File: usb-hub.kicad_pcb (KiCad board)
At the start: 4 copper layers, 23.4 x 28.4 mm, 64 parts, among them J1 USB_C_Receptacle_16pin, J2 USB_C_Receptacle_16pin, J3 USB_C_Receptacle_16pin, J4 Conn_01x01_Female, J5 Conn_01x01_Female, J6 Conn_01x01_Female, J7 Conn_01x01_Female, Q1 PMOS, -3.6A, 0.02R, Q2 Q_NMOS_GSD 1Amp, SW1 SW_Push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

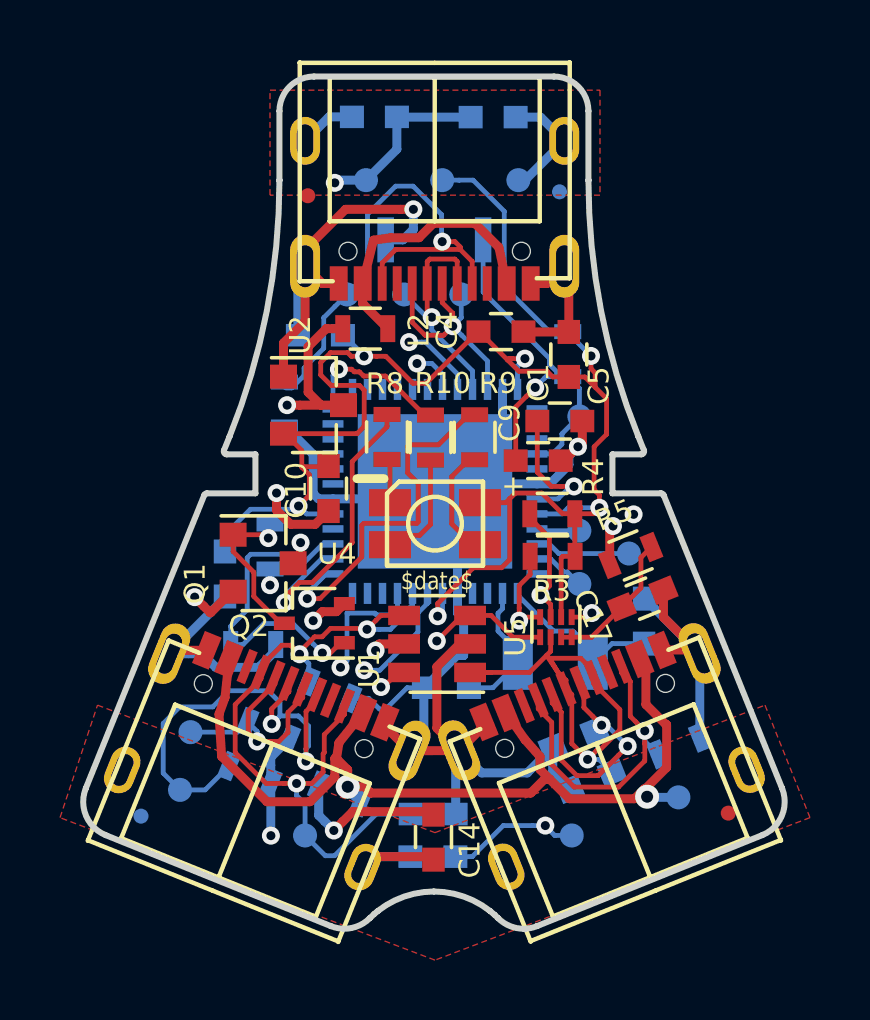
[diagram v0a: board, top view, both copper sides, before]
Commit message: improve clarity of polarity of u5
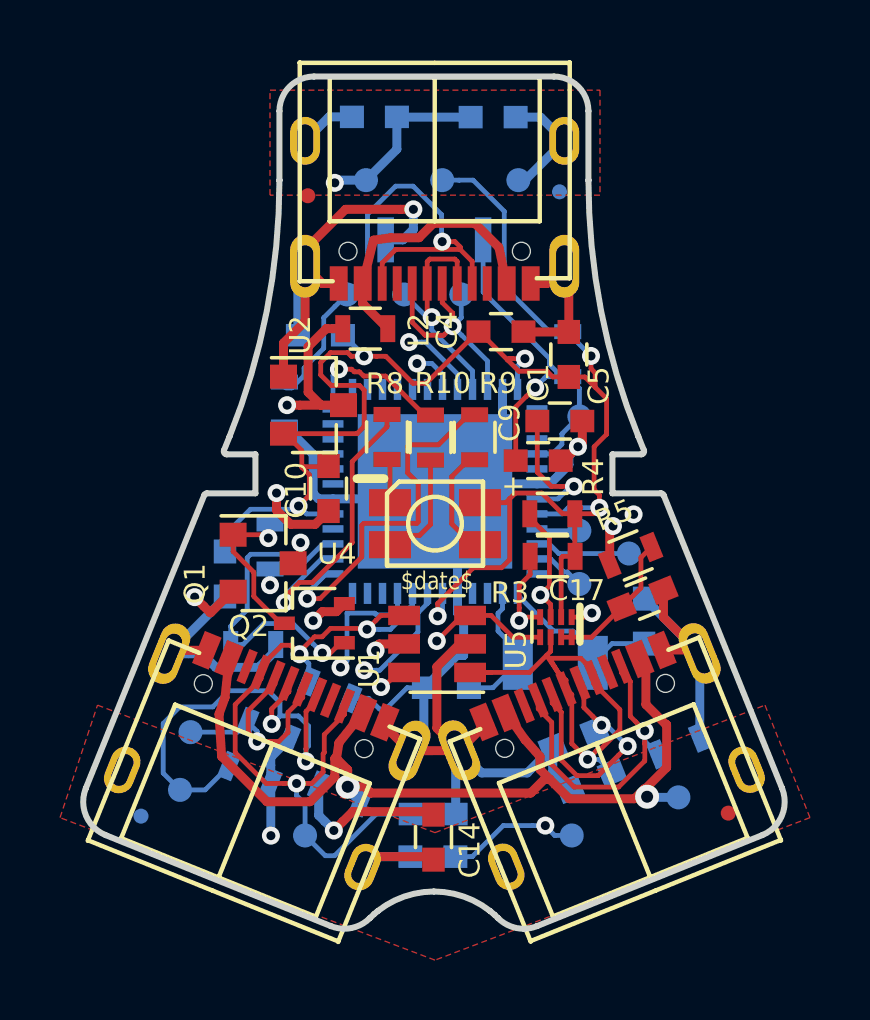
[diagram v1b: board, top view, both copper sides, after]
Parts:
- U5: footprint Housings_SON:X2SON-8_1.4x1mm_Pitch0.35mm -> X2SON-8_1.4x1mm_Pitch0.35mm
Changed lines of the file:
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@@
     (add_net /side-power)
+  )
+  (module X2SON-8_1.4x1mm_Pitch0.35mm (layer F.Cu)
+    (at 146.03 110.15 270)
+    (descr "X2SON-8 1.4x1mm Pitch0.35mm http://www.ti.com/lit/ds/symlink/pca9306.pdf")
+    (tags "X2SON-8 1.4x1mm Pitch0.35mm")
+    (attr smd)
+    (fp_text reference U5 (at 0.75 1.33 90) (layer F.SilkS)
+      (effects (font (size 0.7 0.7) (thickness 0.1)))
+    )
+    (fp_text value pca9306 (at 0 2 270) (layer F.Fab)
+      (effects (font (size 1 1) (thickness 0.15)))
+    )
+    (fp_text user %R (at 0 0) (layer F.Fab)
+      (effects (font (size 0.3 0.3) (thickness 0.05)))
+    )
+    (fp_line (start -0.85 -0.95) (end 0.85 -0.95) (layer F.CrtYd) (width 0.05))
+    (fp_line (start -0.85 0.95) (end -0.85 -0.95) (layer F.CrtYd) (width 0.05))
+    (fp_line (start 0.85 0.95) (end -0.85 0.95) (layer F.CrtYd) (width 0.05))
+    (fp_line (start 0.85 -0.95) (end 0.85 0.95) (layer F.CrtYd) (width 0.05))
+    (fp_line (start 0.5 0.8) (end -0.5 0.8) (layer F.SilkS) (width 0.12))
+    (fp_line (start 0.5 -0.8) (end -0.7 -0.8) (layer F.SilkS) (width 0.25))
+    (fp_line (start 0 -0.7) (end -0.5 -0.2) (layer F.Fab) (width 0.1))
+    (fp_line (start 0 -0.7) (end 0.5 -0.7) (layer F.Fab) (width 0.1))
+    (fp_line (start -0.5 0.7) (end -0.5 -0.2) (layer F.Fab) (width 0.1))
+    (fp_line (start 0.5 0.7) (end -0.5 0.7) (layer F.Fab) (width 0.1))
+    (fp_line (start 0.5 -0.7) (end 0.5 0.7) (layer F.Fab) (width 0.1))
+    (pad 1 smd rect (at -0.335 -0.525 180) (size 0.2 0.53) (layers F.Cu F.Paste F.Mask)
+      (net 1 Earth))
+    (pad 2 smd rect (at -0.335 -0.175 180) (size 0.2 0.53) (layers F.Cu F.Paste F.Mask)
+      (net 3 +3V3))
+    (pad 3 smd rect (at -0.335 0.175 180) (size 0.2 0.53) (layers F.Cu F.Paste F.Mask)
+      (net 58 /scl33))
+    (pad 4 smd rect (at -0.335 0.525 180) (size 0.2 0.53) (layers F.Cu F.Paste F.Mask)
+      (net 57 /sda33))
+    (pad 5 smd rect (at 0.335 0.525 180) (size 0.2 0.53) (layers F.Cu F.Paste F.Mask)
+      (net 22 /sda))
+    (pad 6 smd rect (at 0.335 0.175 180) (size 0.2 0.53) (layers F.Cu F.Paste F.Mask)
+      (net 23 /scl))
+    (pad 7 smd rect (at 0.335 -0.175 180) (size 0.2 0.53) (layers F.Cu F.Paste F.Mask)
+      (net 56 "Net-(C17-Pad2)"))
+    (pad 8 smd rect (at 0.335 -0.525 180) (size 0.2 0.53) (layers F.Cu F.Paste F.Mask)
+      (net 56 "Net-(C17-Pad2)"))
+    (model ${KISYS3DMOD}/Housings_SON.3dshapes/X2SON-8_1.4x1mm_Pitch0.35mm.wrl
+      (at (xyz 0 0 0))
+      (scale (xyz 1 1 1))
+      (rotate (xyz 0 0 0))
+    )
   )
   (module raise_fp:usb-c-16smt (layer F.Cu)
@@
     (tags "resistor 0603")
     (attr smd)
-    (fp_text reference R3 (at -0.03 1.15) (layer F.SilkS)
+    (fp_text reference R3 (at -1.42 1.21) (layer F.SilkS)
       (effects (font (size 0.7 0.7) (thickness 0.1)))
     )
@@
     (tags "capacitor 0603")
     (attr smd)
-    (fp_text reference C17 (at 1.776907 0.060011 292) (layer F.SilkS)
+    (fp_text reference C17 (at 1.932152 1.077237 180) (layer F.SilkS)
       (effects (font (size 0.7 0.7) (thickness 0.1)))
     )
@@
       (net 23 /scl))
     (model ${KIPRJMOD}/raise_fp.pretty/models/R_0603_1608Metric.wrl
-      (at (xyz 0 0 0))
-      (scale (xyz 1 1 1))
-      (rotate (xyz 0 0 0))
-    )
-  )
-  (module Housings_SON:X2SON-8_1.4x1mm_Pitch0.35mm (layer F.Cu)
-    (at 146.03 110.15 270)
-    (descr "X2SON-8 1.4x1mm Pitch0.35mm http://www.ti.com/lit/ds/symlink/pca9306.pdf")
-    (tags "X2SON-8 1.4x1mm Pitch0.35mm")
-    (attr smd)
-    (fp_text reference U5 (at 0.33 1.35 90) (layer F.SilkS)
-      (effects (font (size 0.7 0.7) (thickness 0.1)))
-    )
-    (fp_text value pca9306 (at 0 2 270) (layer F.Fab)
-      (effects (font (size 1 1) (thickness 0.15)))
-    )
-    (fp_text user %R (at 0 0) (layer F.Fab)
-      (effects (font (size 0.3 0.3) (thickness 0.05)))
-    )
-    (fp_line (start -0.85 -0.95) (end 0.85 -0.95) (layer F.CrtYd) (width 0.05))
-    (fp_line (start -0.85 0.95) (end -0.85 -0.95) (layer F.CrtYd) (width 0.05))
-    (fp_line (start 0.85 0.95) (end -0.85 0.95) (layer F.CrtYd) (width 0.05))
-    (fp_line (start 0.85 -0.95) (end 0.85 0.95) (layer F.CrtYd) (width 0.05))
-    (fp_line (start 0.5 0.8) (end -0.5 0.8) (layer F.SilkS) (width 0.12))
-    (fp_line (start 0.5 -0.8) (end -0.7 -0.8) (layer F.SilkS) (width 0.12))
-    (fp_line (start 0 -0.7) (end -0.5 -0.2) (layer F.Fab) (width 0.1))
-    (fp_line (start 0 -0.7) (end 0.5 -0.7) (layer F.Fab) (width 0.1))
-    (fp_line (start -0.5 0.7) (end -0.5 -0.2) (layer F.Fab) (width 0.1))
-    (fp_line (start 0.5 0.7) (end -0.5 0.7) (layer F.Fab) (width 0.1))
-    (fp_line (start 0.5 -0.7) (end 0.5 0.7) (layer F.Fab) (width 0.1))
-    (pad 1 smd rect (at -0.335 -0.525 180) (size 0.2 0.53) (layers F.Cu F.Paste F.Mask)
-      (net 1 Earth))
-    (pad 2 smd rect (at -0.335 -0.175 180) (size 0.2 0.53) (layers F.Cu F.Paste F.Mask)
-      (net 3 +3V3))
-    (pad 3 smd rect (at -0.335 0.175 180) (size 0.2 0.53) (layers F.Cu F.Paste F.Mask)
-      (net 58 /scl33))
-    (pad 4 smd rect (at -0.335 0.525 180) (size 0.2 0.53) (layers F.Cu F.Paste F.Mask)
-      (net 57 /sda33))
-    (pad 5 smd rect (at 0.335 0.525 180) (size 0.2 0.53) (layers F.Cu F.Paste F.Mask)
-      (net 22 /sda))
-    (pad 6 smd rect (at 0.335 0.175 180) (size 0.2 0.53) (layers F.Cu F.Paste F.Mask)
-      (net 23 /scl))
-    (pad 7 smd rect (at 0.335 -0.175 180) (size 0.2 0.53) (layers F.Cu F.Paste F.Mask)
-      (net 56 "Net-(C17-Pad2)"))
-    (pad 8 smd rect (at 0.335 -0.525 180) (size 0.2 0.53) (layers F.Cu F.Paste F.Mask)
-      (net 56 "Net-(C17-Pad2)"))
-    (model ${KISYS3DMOD}/Housings_SON.3dshapes/X2SON-8_1.4x1mm_Pitch0.35mm.wrl
       (at (xyz 0 0 0))
       (scale (xyz 1 1 1))
@@
   (segment (start 147.220567 110.485) (end 148.224612 109.480955) (width 0.16) (layer F.Cu) (net 56))
   (segment (start 146.205 110.485) (end 146.555 110.485) (width 0.16) (layer F.Cu) (net 56))
-  (via (at 144.806272 109.932582) (size 0.6) (drill 0.3) (layers F.Cu B.Cu) (net 57) (status 1000000))
+  (via (at 144.806272 109.932582) (size 0.6) (drill 0.3) (layers F.Cu B.Cu) (net 57))
   (via (at 141.40059 101.360783) (size 0.6) (drill 0.3) (layers F.Cu B.Cu) (net 57))
   (segment (start 145.17 108.4) (end 144.806272 108.763728) (width 0.16) (layer F.Cu) (net 57))

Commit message: esd fixes: remove adc connections, protect usb +-, move esd protection
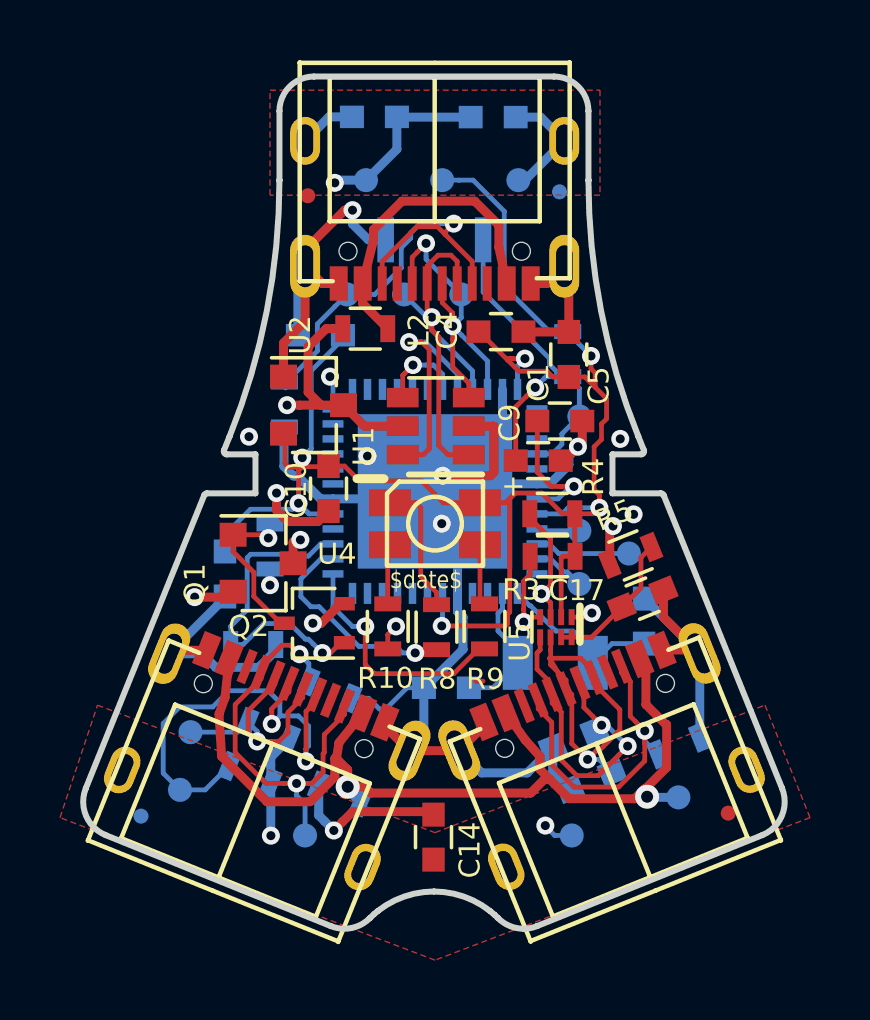
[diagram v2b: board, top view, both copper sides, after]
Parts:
- removed C15, C16: 100pF ceramic, 100v, 10%, raise_fp:C_0603
- moved U1 7.26 mm to (142.0, 103.5)
- moved R8 6.55 mm to (142.1, 110.2), turned to 270 degrees
- moved R10 6.45 mm to (140.4, 110.1), turned to 270 degrees
- moved R9 6.31 mm to (143.7, 110.1), turned to 270 degrees
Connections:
- U1 pad 1: /scl -> /usb-up_N
- U1 pad 3: /sda -> /usb-up_P
- U1 pad 4: /dfp-l-cc -> /sda33
- U1 pad 6: /dfp-r-cc -> /scl33
- U3 pad 7: /ufp-cc -> Net-(U3-Pad7)
- U3 pad 8: /dfp-l-cc -> Net-(U3-Pad8)
- U3 pad 9: /dfp-r-cc -> Net-(U3-Pad9)
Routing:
- net /ufp-cc: track 36.1 -> 14.9 mm, vias 2 -> 1
- net /dfp-r-cc: track 36.6 -> 16.9 mm, vias 4 -> 2
- net /dfp-l-cc: track 24.7 -> 13.9 mm, vias 3 -> 2
- net /sda: track 50.5 -> 40.9 mm, vias 4 -> 3
- net Earth: track 110.0 -> 102.1 mm, vias 6 -> 11
- net /pwm1_b: track 5.09 -> 11.2 mm, vias 1 -> 2
- net /usb-up_N: track 7.93 -> 13.4 mm
- net /scl33: track 17.0 -> 22.0 mm
- net +5V: track 76.5 -> 72.5 mm, vias 7 -> 6
- net /pwm1_g: track 12.0 -> 8.16 mm
- net /scl: track 51.1 -> 47.4 mm
- net /usb-up_P: track 8.28 -> 11.7 mm, vias 1 -> 2
- net Net-(R8-Pad1): track 1.48 -> 4.55 mm
- net /pwm1_r: track 10.3 -> 7.29 mm
- net Net-(R9-Pad1): track 3.80 -> 2.29 mm
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
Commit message: remove tiny translator and go back to 2 mosfets, also fix farnell number on 2.7k R
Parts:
- removed C17: 100pF ceramic, 100v, 10%, raise_fp:C_0603
- removed R5: 200k, 125mW, 5%, raise_fp:R_0603
- removed U5: pca9306, X2SON-8_1.4x1mm_Pitch0.35mm
- added Q3: Q_NMOS_GSD 1Amp, raise_fp:SOT-323_SC-70, F.Cu at (148.5, 107.7)
- added Q4: Q_NMOS_GSD 1Amp, raise_fp:SOT-323_SC-70, F.Cu at (146.1, 109.9)
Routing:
- net +5V: track 72.5 -> 51.6 mm, vias 6 -> 5
- net /scl: track 47.4 -> 52.7 mm
- net Net-(C17-Pad2): track 4.85 -> 0.00 mm
- net /scl33: track 22.0 -> 26.5 mm
- net Earth: track 102.1 -> 98.7 mm, vias 11 -> 9
- net /sda33: track 15.8 -> 17.4 mm
- net /sda: track 40.9 -> 42.2 mm

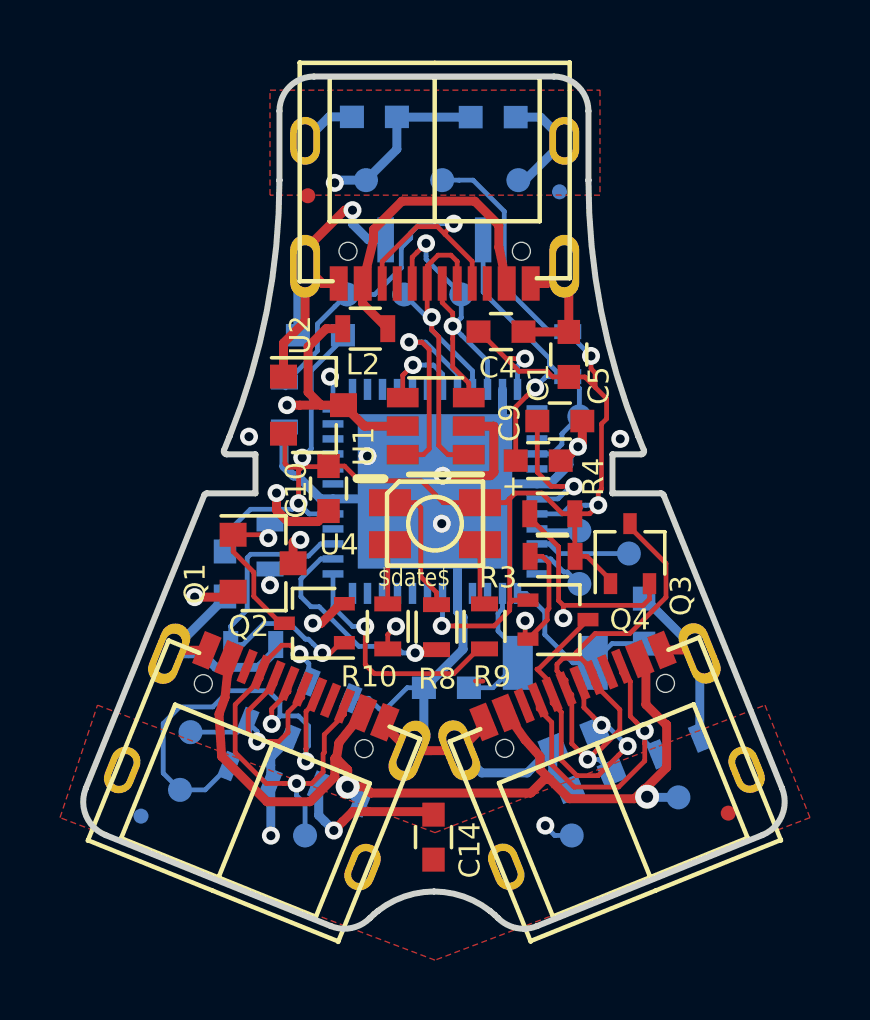
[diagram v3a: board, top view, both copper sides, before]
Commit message: thickened power traces
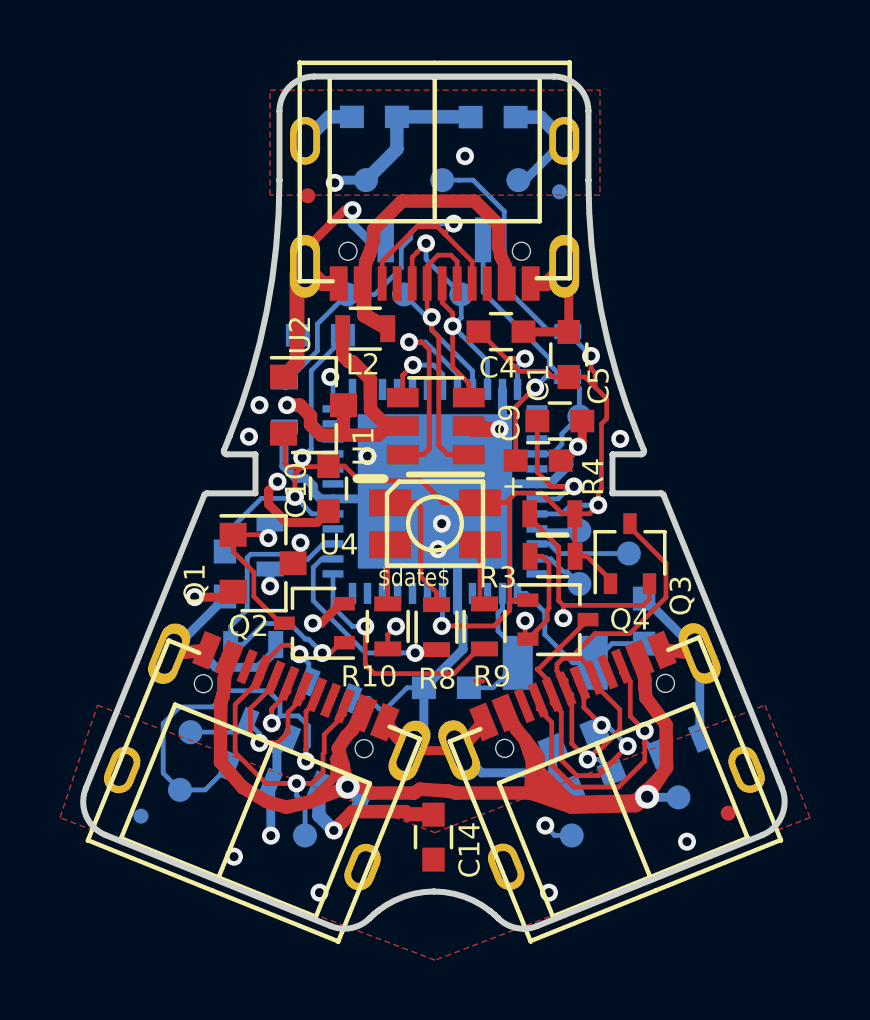
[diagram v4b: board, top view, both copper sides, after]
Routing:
- net /side-power: track 32.6 -> 46.4 mm
- net +5V: track 51.6 -> 61.6 mm
- net /side-power-pre-ferrite: track 19.0 -> 21.6 mm
- net Earth: track 98.7 -> 96.5 mm, vias 9 -> 16
- net Net-(J1-PadA4/B9): track 10.6 -> 11.9 mm
- net /pwm1_r: track 7.29 -> 6.77 mm

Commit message: few more gnd vias for the high speed tracks
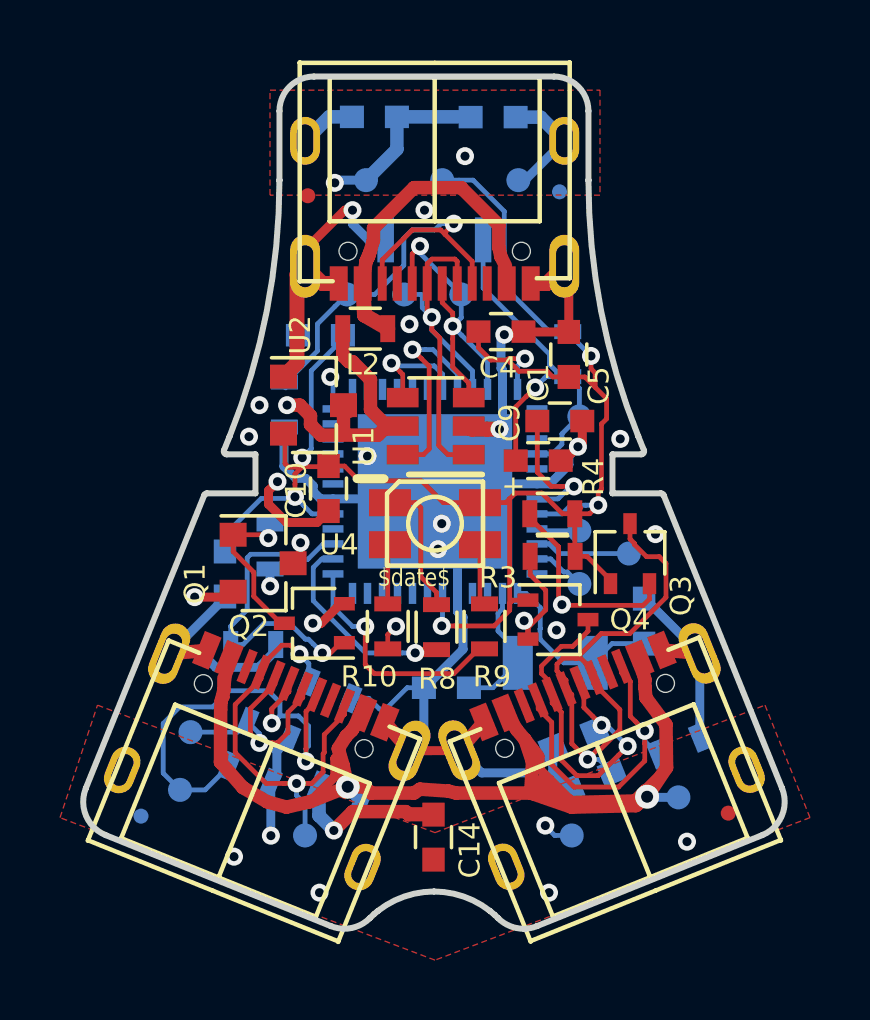
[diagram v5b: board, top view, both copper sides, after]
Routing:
- net Earth: track 96.5 -> 111.0 mm, vias 16 -> 21
- net /scl33: track 26.5 -> 24.4 mm
- net /sda33: track 17.4 -> 18.4 mm
